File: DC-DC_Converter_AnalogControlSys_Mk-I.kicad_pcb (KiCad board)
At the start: 2 copper layers, 100 x 57 mm, 44 parts, among them J1 Conn_01x06, J2 Conn_01x03, J3 TRIAmpTestPoint, J4 SQRTestPoint, Q1 OSP120N04T, U1 TL054CN, U2 TL054CN

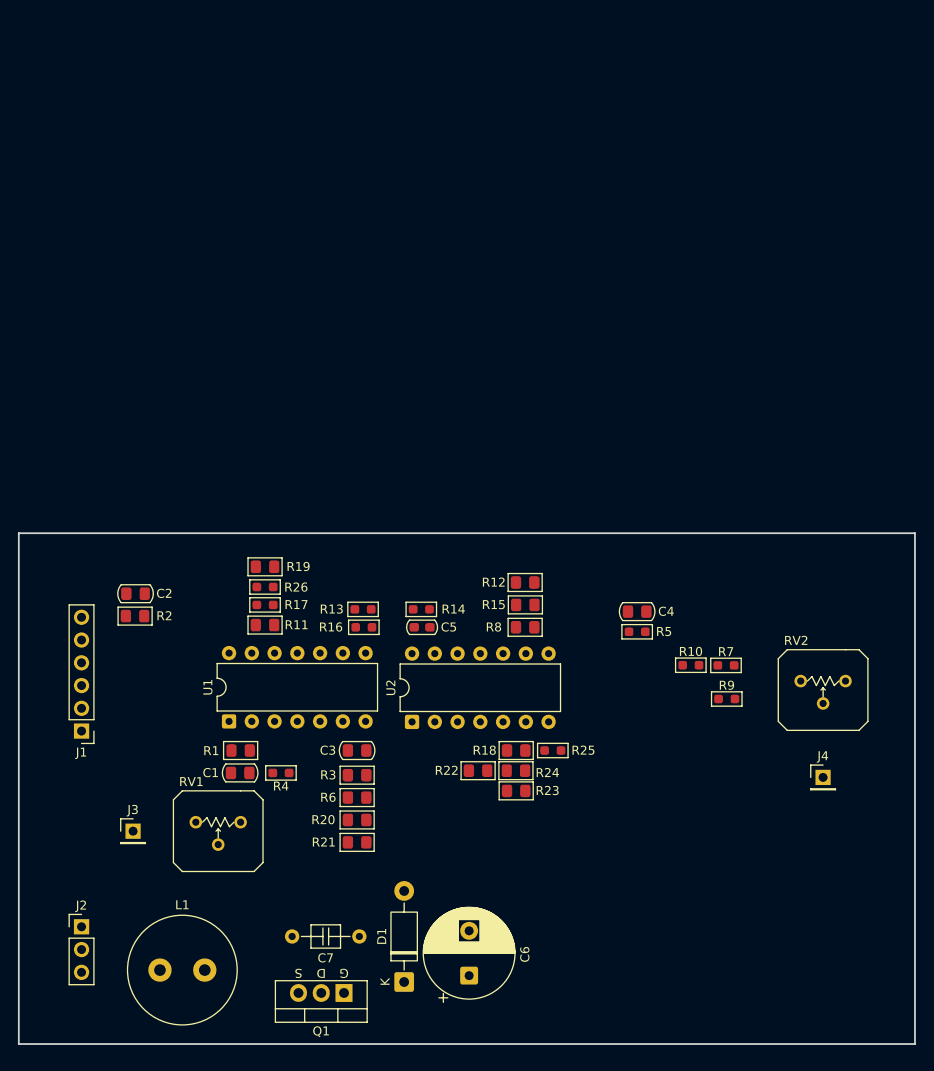
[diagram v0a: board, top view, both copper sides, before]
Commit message: DONE PCB layout and routing. TODO add some silkscreen text, double-check everything, then organize BOM and JLCPCB order.
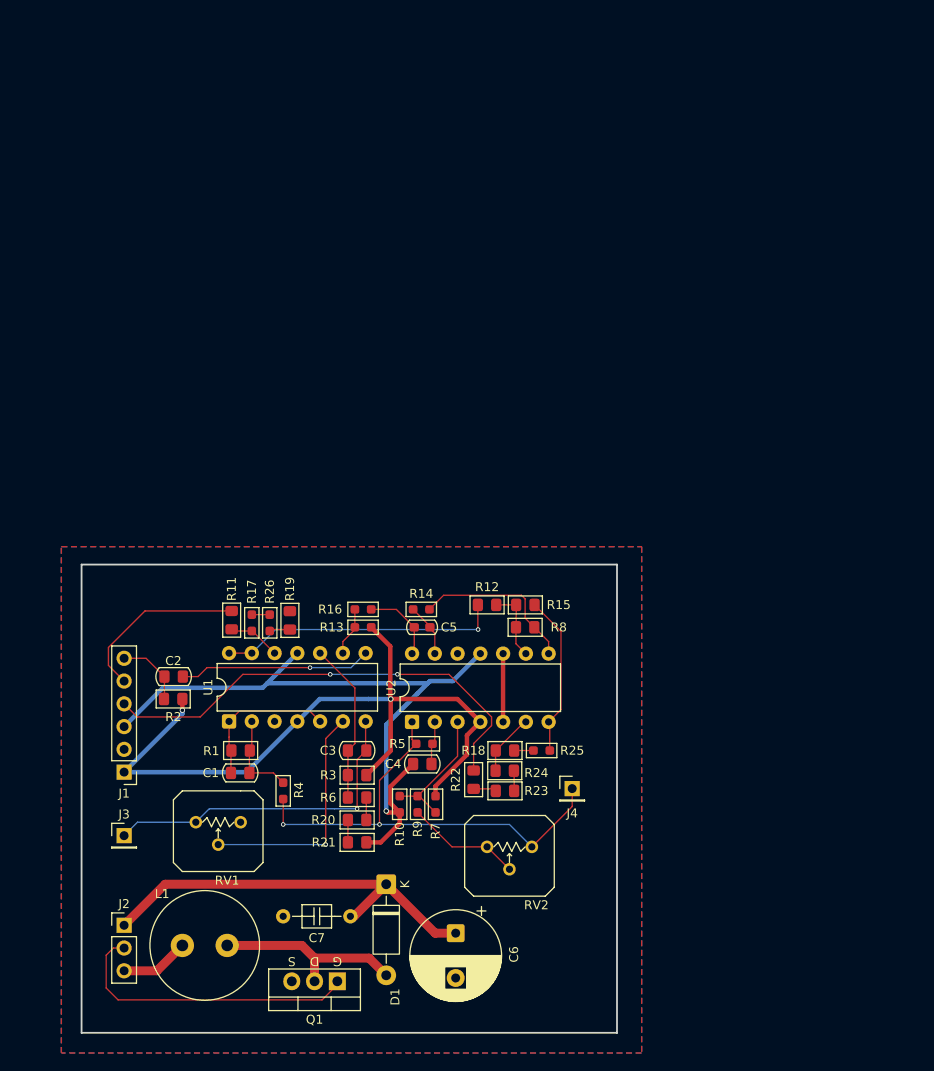
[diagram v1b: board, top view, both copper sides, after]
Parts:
- moved RV2 39.6 mm to (103.8, 124.5)
- moved R9 36.4 mm to (93.5, 117.2), turned to -90 degrees
- moved R10 36.0 mm to (91.5, 117.2), turned to 90 degrees
- moved R7 35.9 mm to (95.5, 117.2), turned to 90 degrees
- moved C4 29.4 mm to (94.0, 112.8), turned to 0 degrees
- moved J4 28.0 mm to (110.8, 115.5)
- moved R5 26.8 mm to (94.2, 110.5), turned to 180 degrees
- moved D1 11.1 mm to (90.0, 126.2), turned to -90 degrees
- moved C2 10.2 mm to (66.3, 103.0)
- moved R2 10.2 mm to (66.2, 105.5)
- moved J1 6.60 mm to (60.8, 113.7)
- moved R19 6.59 mm to (79.2, 96.7), turned to 90 degrees
- moved C6 4.97 mm to (97.8, 131.6), turned to -90 degrees
- moved R12 4.93 mm to (101.2, 95.0)
- moved J2 4.75 mm to (60.8, 130.8)
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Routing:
- net +5V: track 0.00 -> 83.9 mm, vias 0 -> 2
- net -5V: track 0.00 -> 78.4 mm, vias 0 -> 1
- net SQR_W: track 0.00 -> 53.3 mm, vias 0 -> 2
- net targ_in: track 0.00 -> 52.9 mm, vias 0 -> 2
- net /5x_BoostConverter_Mk-I/V_out: track 0.00 -> 46.6 mm
- net Net-(J3-Pin_1): track 0.00 -> 37.4 mm, vias 0 -> 1
- net /5x_BoostConverter_Mk-I/V_ctrl_in: track 0.00 -> 33.4 mm
- net Net-(U1D--): track 0.00 -> 31.6 mm, vias 0 -> 1
- net Net-(U1B--): track 0.00 -> 26.5 mm, vias 0 -> 1
- net Net-(D1-A): track 0.00 -> 21.7 mm
- net Net-(C2-Pad1): track 0.00 -> 21.5 mm, vias 0 -> 1
- net conv_in: track 0.00 -> 19.9 mm
- net Net-(R14-Pad2): track 0.00 -> 18.7 mm
- net Net-(R15-Pad1): track 0.00 -> 18.1 mm
- net Net-(U1C-+): track 0.00 -> 18.0 mm
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- added copper zone on B.Cu, net GND
- added copper zone on F.Cu, net GND
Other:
- board size 100 x 57 mm -> 59.8 x 52.2 mm

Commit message: ADDED silkscreen graphics. DONE all checks on PCB validity. TODO double-check schematic, find suitable replacement for TL054, then order PCB and parts.
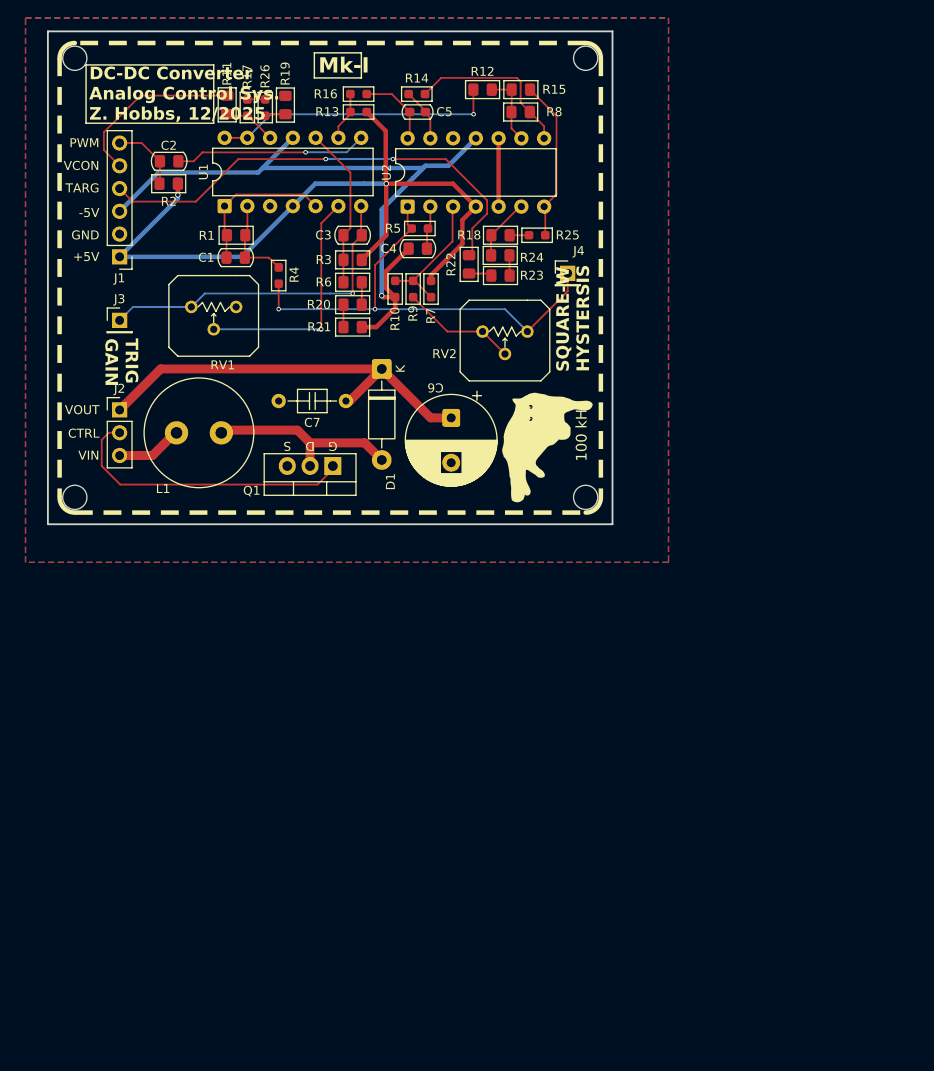
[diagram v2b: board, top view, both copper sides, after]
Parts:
- added G***: LOGO, bird, F.Cu at (84.7, 61.8)
- added G***: LOGO, ZCustomFootprints:flufftest_3, F.Cu at (107.0, 73.5)
- moved C6 57.5 mm to (97.2, 74.1)
- moved U2 57.5 mm to (92.4, 50.6)
- moved C1 57.5 mm to (73.2, 56.2)
- moved C2 57.5 mm to (65.8, 45.5)
- moved C3 57.5 mm to (86.2, 53.8)
- moved C4 57.5 mm to (93.5, 55.2)
- moved C5 57.5 mm to (93.5, 40.0)
- moved C7 57.5 mm to (85.5, 72.2)
- moved D1 57.5 mm to (89.5, 68.7)
- moved J1 57.5 mm to (60.2, 56.2)
- moved J2 57.5 mm to (60.2, 73.2)
- moved J3 57.5 mm to (60.2, 63.2)
- moved J4 57.5 mm to (110.2, 58.0)
- moved Q1 57.5 mm to (84.0, 79.5)
- moved R1 57.5 mm to (73.2, 53.8)
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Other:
- board size 59.8 x 52.2 mm -> 63 x 55 mm
- board text added: "+5V"
- board text added: "-5V"
- board text added: "100 kHz"
- board text added: "CTRL"
- board text added: "DC-DC Converter Analog Control Sys. Z. Hobbs, 12/2025"
- board text added: "GND"
- board text added: "Live, Laugh, Laplace Transform"
- board text added: "Mk-I"
- board text added: "PWM"
- board text added: "SQUARE-W HYSTERSIS"
- board text added: "TARG"
- board text added: "TRIG GAIN"
- board text added: "VCON"
- board text added: "VIN"
- board text added: "VOUT"
